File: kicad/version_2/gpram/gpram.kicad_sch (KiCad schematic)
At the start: 55 parts

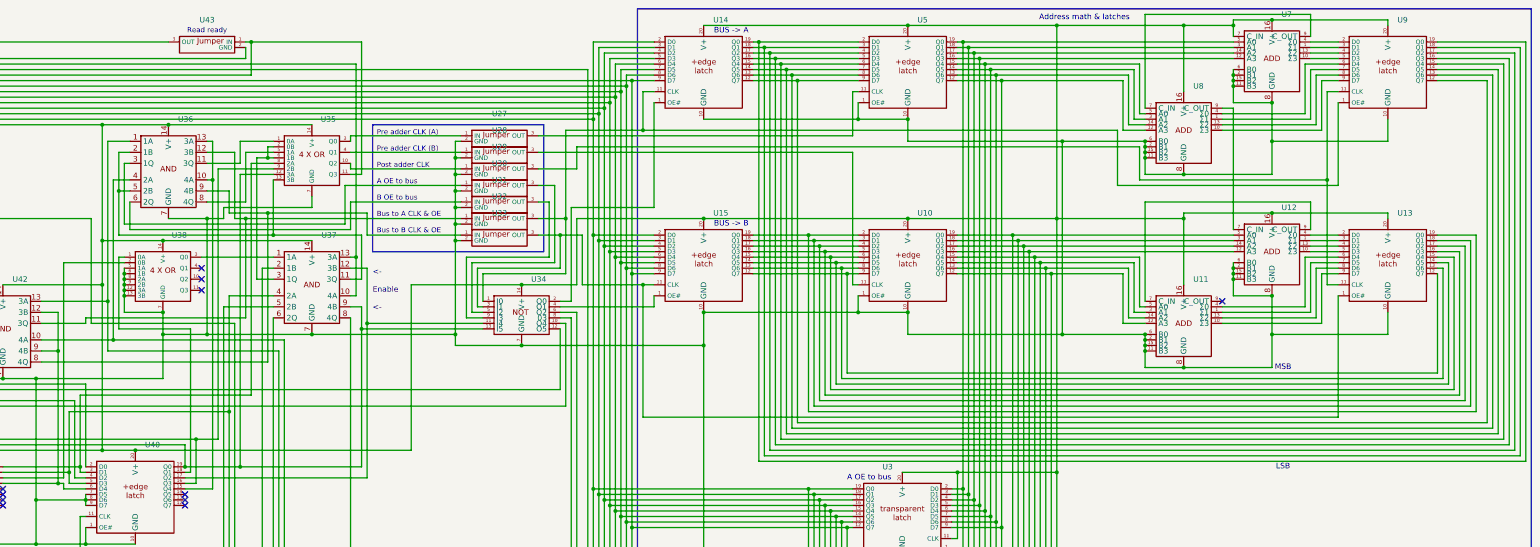
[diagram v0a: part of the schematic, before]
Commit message: Added compiler functionality to deal with stack offset
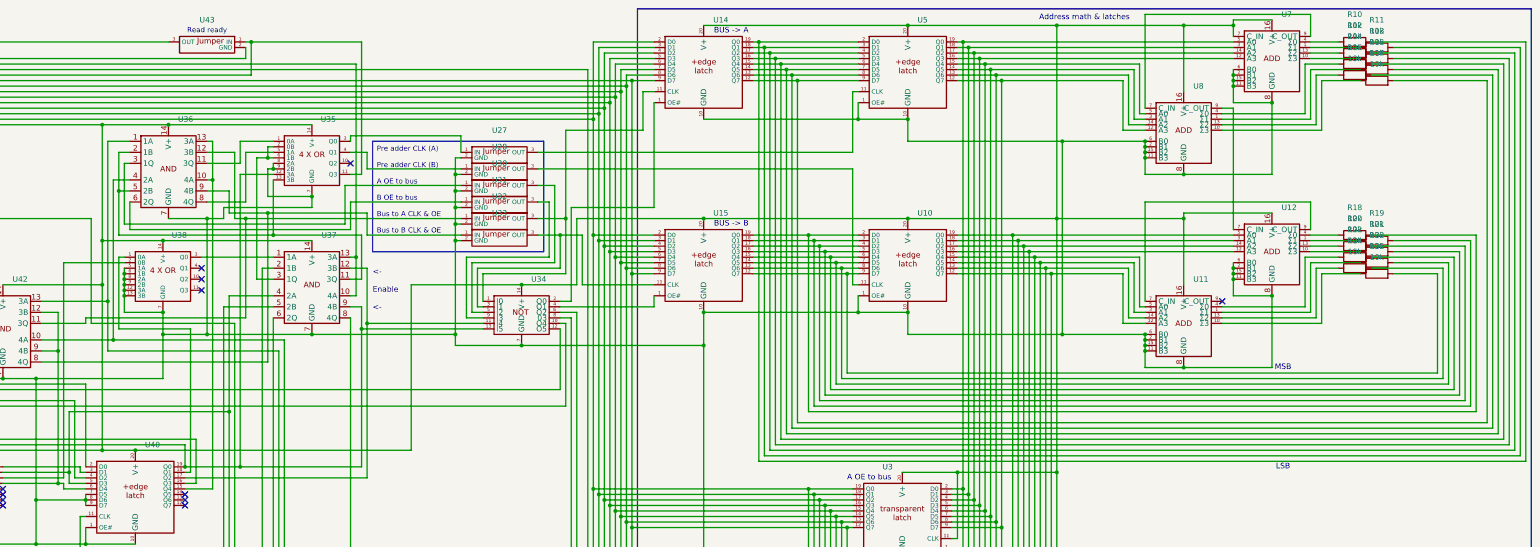
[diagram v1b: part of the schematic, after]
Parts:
- removed U13, U9: ~, Package_DIP:DIP-20_W7.62mm, symbol custom_symbol_lib:rising_edge_8_bit_latch
- removed U29: ~, custom_footprint_library:jumper, symbol custom_symbol_lib:jumper
- added R10, R11, R12, R13, R14, R15, R16, R17, R18, R19, R20, R21, R22, R23, R24, R25: 10k, custom_footprint_library:0.4_pitch_resistor, symbol Device:R
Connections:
- net at R1.2, R2.2, R3.2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: now also U35.8 (2A), U35.9 (2B)
- net at U14.12 (Q7), U5.9 (D7): now also R17.2
- net at U14.13 (Q6), U5.8 (D6): now also R16.2
- net at U14.14 (Q5), U5.7 (D5): now also R15.2
- net at U14.15 (Q4), U5.6 (D4): now also R14.2
- net at U14.16 (Q3), U5.5 (D3): now also R13.2
- net at U14.17 (Q2), U5.4 (D2): now also R12.2
- net at U14.18 (Q1), U5.3 (D1): now also R11.2
- net at U14.19 (Q0), U5.2 (D0): now also R10.2
- net at U10.9 (D7), U15.12 (Q7): now also R25.2
- net at U10.8 (D6), U15.13 (Q6): now also R24.2
- net at U10.7 (D5), U15.14 (Q5): now also R23.2
- net at U10.6 (D4), U15.15 (Q4): now also R22.2
- net at U10.5 (D3), U15.16 (Q3): now also R21.2
- net at U10.4 (D2), U15.17 (Q2): now also R20.2
- net at U10.3 (D1), U15.18 (Q1): now also R19.2
- net at U10.2 (D0), U15.19 (Q0): now also R18.2
- net at U11.1 (Σ1): now also R23.1
- net at U11.10 (Σ3): now also R25.1
- net at U11.13 (Σ2): now also R24.1
- net at U11.4 (Σ0): now also R22.1
- net at U12.1 (Σ1): now also R19.1
- net at U12.10 (Σ3): now also R21.1
- net at U12.13 (Σ2): now also R20.1
- net at U12.4 (Σ0): now also R18.1
- net at U39.19 (Q0), U40.3 (D1): no longer U35.8 (2A)
- net at U39.4 (D2), U40.16 (Q3): no longer U35.9 (2B)
- net at U7.1 (Σ1): now also R11.1
- net at U7.10 (Σ3): now also R13.1
- net at U7.13 (Σ2): now also R12.1
- net at U7.4 (Σ0): now also R10.1
- net at U8.4 (Σ0): now also R14.1
- net at U8.1 (Σ1): now also R15.1
- net at U8.13 (Σ2): now also R16.1
- net at U8.10 (Σ3): now also R17.1
- no-connect marks 18 -> 19
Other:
- moved on the sheet: U27, U28
